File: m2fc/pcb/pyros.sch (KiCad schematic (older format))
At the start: 51 parts, among them P501 CONN_2, P502 CONN_2, P503 CONN_2, Q501 MOSFET_P, Q502 MOSFET_N, Q503 MOSFET_P, Q504 MOSFET_N, Q505 MOSFET_P, Q506 MOSFET_N, U501 HOUSING, U502 HOUSING, U503 HOUSING

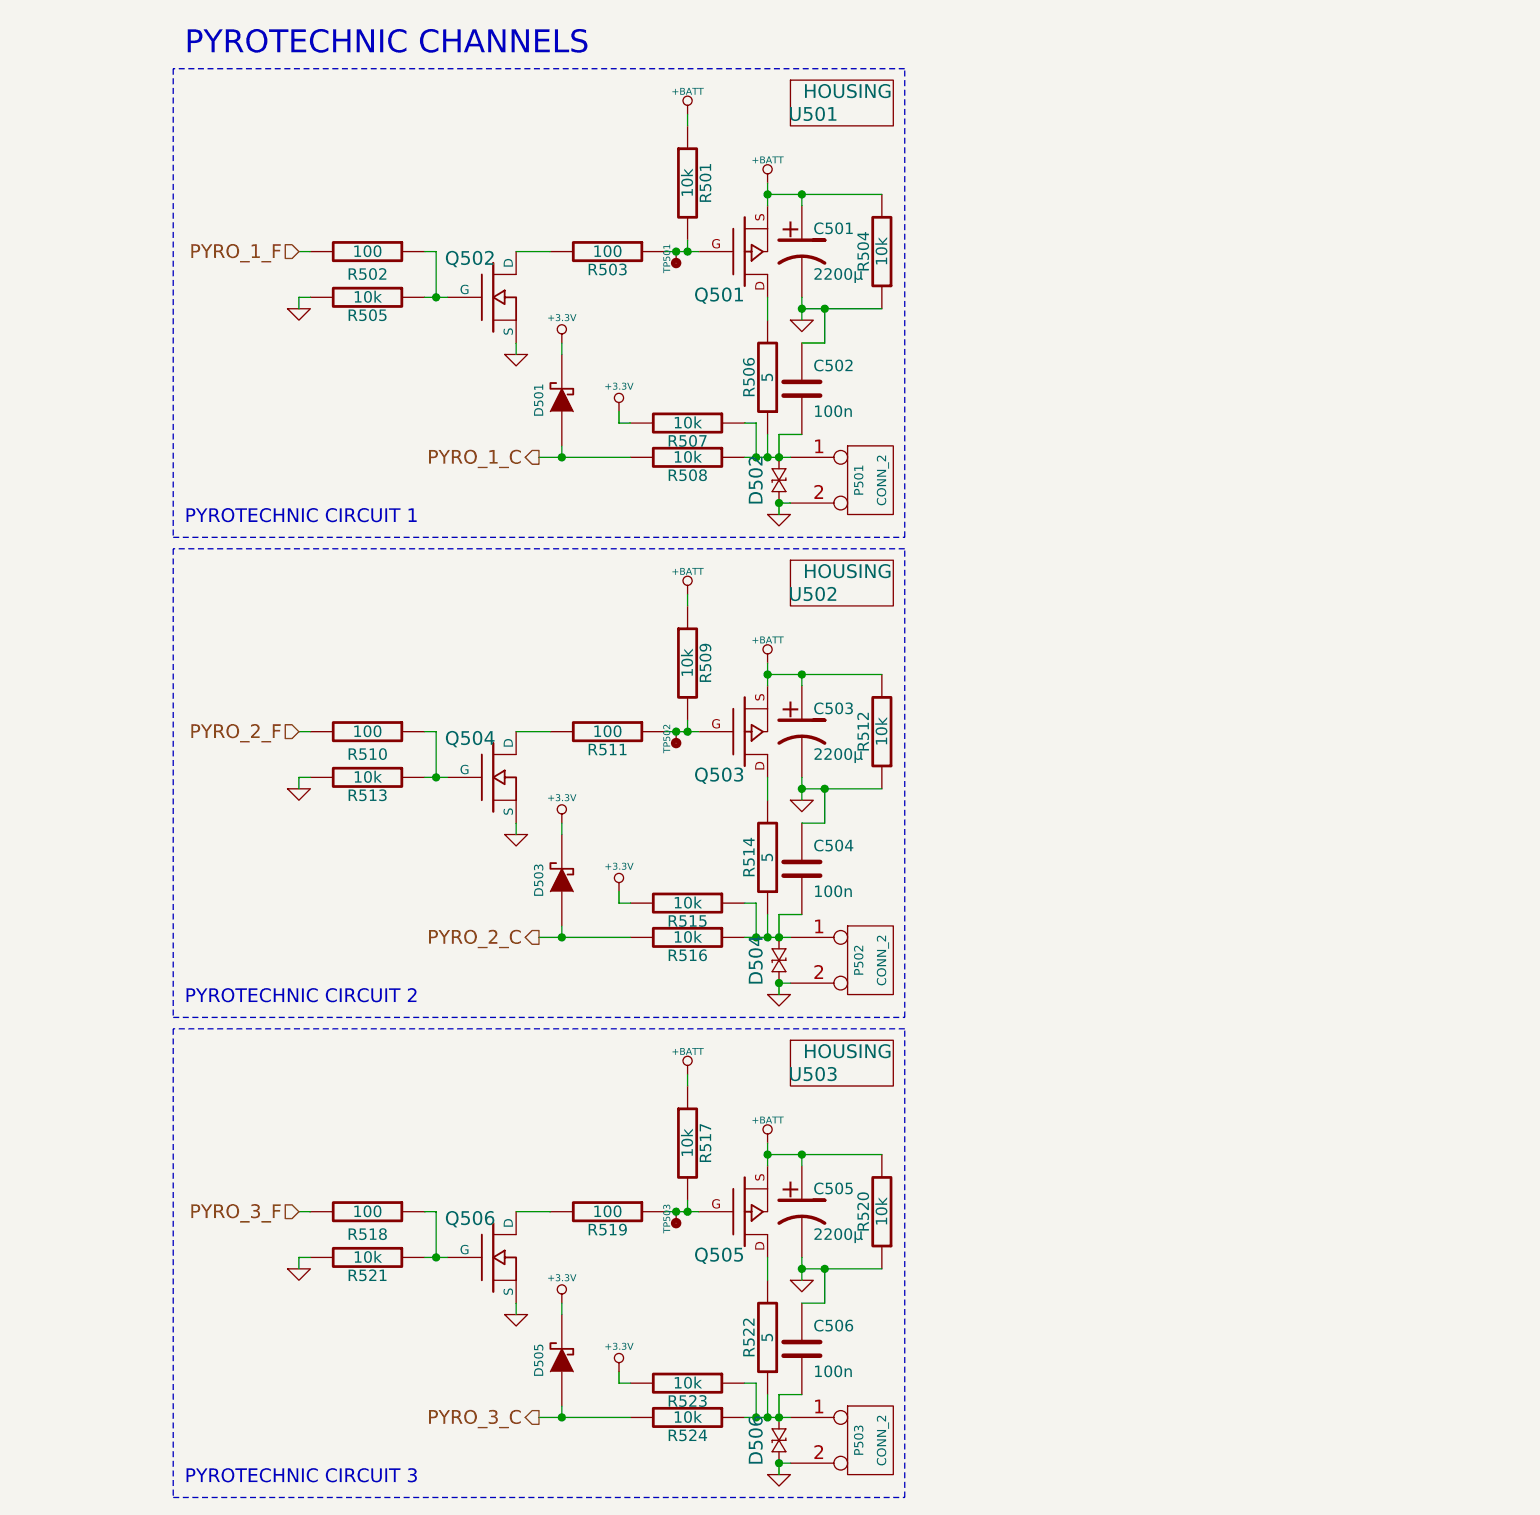
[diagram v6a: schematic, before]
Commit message: m2fc footprints, start layout
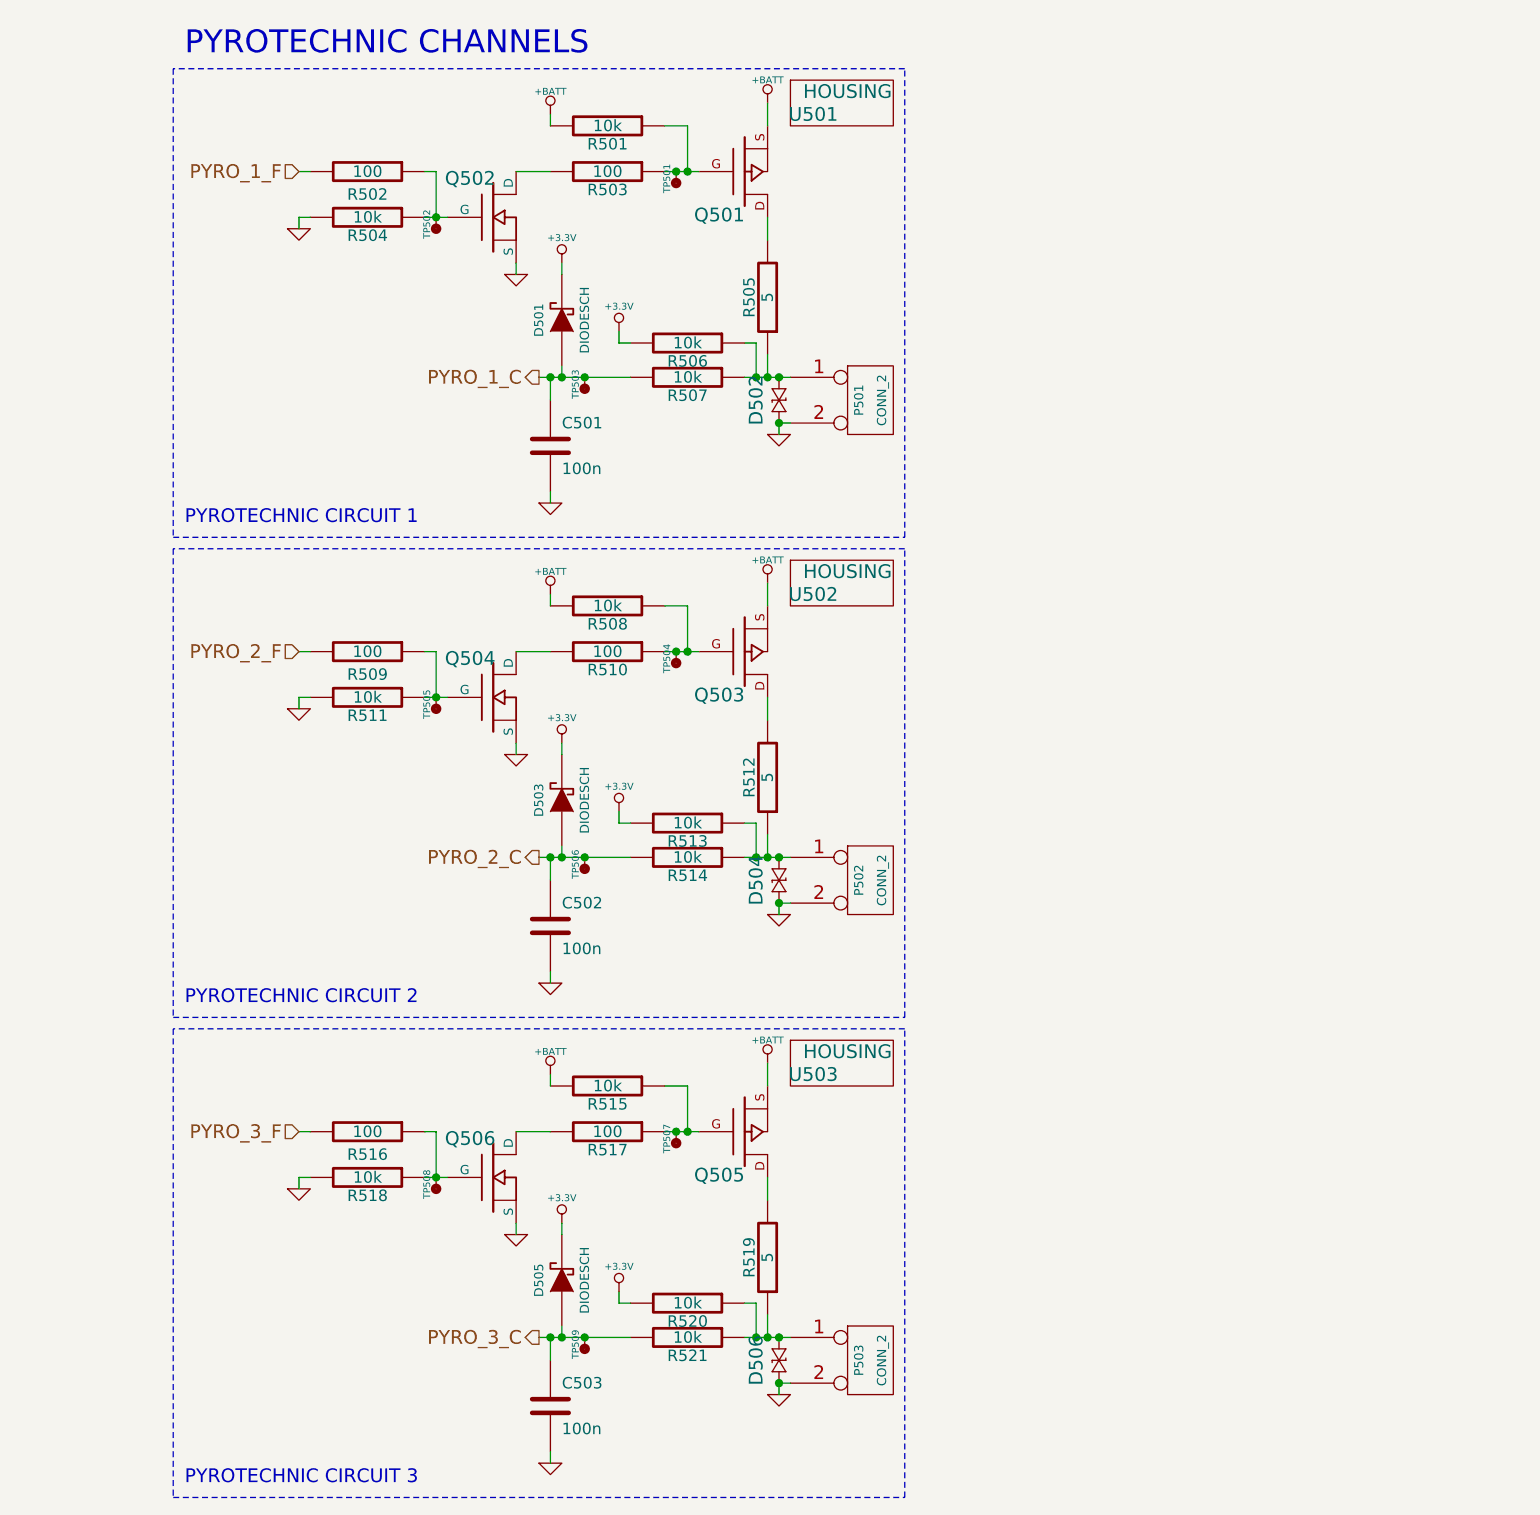
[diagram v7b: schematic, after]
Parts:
- removed C501, C503, C505: 2200µ, symbol CP1
- removed C504, C506: 100n, m2fc:C0603, symbol C
- removed R504, R523, R524: 10k, m2fc:R0603, symbol R
- removed R522: 5, symbol R
- added C501, C503: 100n, m2fc:C0603, symbol C
- added R508: 10k, m2fc:R0603, symbol R
- added TP504, TP505, TP506, TP507, TP508, TP509: TESTPAD, m2fc:TESTPAD, symbol TESTPAD
- D501, D503, D505: footprint SOT-23 -> m2fc:SOD323; Farnell 1056832 -> 1349646
- Q501, Q502, Q503, Q504, Q505, Q506: footprint SOT-23 -> m2fc:SOT-23
- R505: renamed from R506; footprint (none) -> m2fc:PWR4318
- R509, R516, R517: value 10k -> 100; Farnell 2332016 -> 2331989
- R511, R518: value 100 -> 10k; Farnell 2331989 -> 2332016
- R512: value 10k -> 5; footprint m2fc:R0603 -> m2fc:PWR4318; Farnell 2332016 -> 2328356
- R514: value 5 -> 10k; footprint (none) -> m2fc:R0603; Farnell 2328356 -> 2332016
- R519: value 100 -> 5; footprint m2fc:R0603 -> m2fc:PWR4318; Farnell 2331989 -> 2328356
- renumbered R505 to R504, R507 to R506, R508 to R507
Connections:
- net +3.3V: now also R513.2, R520.2; no longer R515.2
- net +BATT: now also R501.2, R515.2, R508.2; no longer R501.1, R509.1, R512.2, R517.1, R520.2
- net GND: now also C502.2, R511.2, R518.2, C501.2, C503.2; no longer C502.1, R512.1, R513.2, R520.1, R521.2
- net PYRO_1_C: now also TP503.1 (TP), C501.1
- net PYRO_2_C: now also C502.1, R514.2, TP506.1 (TP); no longer R516.2
- net PYRO_2_F: now also R509.2; no longer R510.2
- net PYRO_3_C: now also R521.2, C503.1, TP509.1 (TP)
- net PYRO_3_F: now also R516.2; no longer R518.2
- net at Q502.G, R502.1, R504.1: now also TP502.1 (TP)
- net at D502.1, P501.1 (P1), R505.1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: no longer C502.2
- net at Q501.G, R503.1, TP501.1 (TP): now also R501.1; no longer R501.2
- net at D504.1, P502.1 (P1), R514.1: now also R512.1, R513.1; no longer R515.1, R516.1
- net at Q503.D: now also R512.2; no longer R514.2
- net at Q504.D: now also R510.2; no longer R511.2
- net at Q506.G, R518.1: now also R516.1, TP508.1 (TP); no longer R521.1
- net at D506.1, P503.1 (P1): now also R519.1, R520.1, R521.1
- net at Q505.D: now also R519.2
- net at Q506.D: now also R517.2; no longer R519.2
- new net: Q504.G, R509.1, R511.1, TP505.1 (TP)
- new net: Q503.G, R508.1, R510.1, TP504.1 (TP)
- new net: Q505.G, R515.1, R517.1, TP507.1 (TP)
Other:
- moved on the sheet: D502, P501, Q501, Q502, R501, R502, R503, R504, R505, R506, R507, TP501

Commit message: paid off woo
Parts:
- Q501, Q502, Q503, Q504, Q505, Q506: footprint m2fc:SOT-23 -> m2fc:SOT-23-MOSFET
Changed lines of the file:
@@
 PYROTECHNIC CIRCUIT 1
 $Comp
-L GND #PWR0148
+L GND #PWR0153
 U 1 1 53B98AB3
 P 3650 1750
-F 0 "#PWR0148" H 3650 1750 30  0001 C CNN
+F 0 "#PWR0153" H 3650 1750 30  0001 C CNN
 F 1 "GND" H 3650 1680 30  0001 C CNN
 F 2 "" H 3650 1750 60  0001 C CNN
@@
 $EndComp
 $Comp
-L GND #PWR0149
+L GND #PWR0154
 U 1 1 53B98AB9
 P 4600 1950
-F 0 "#PWR0149" H 4600 1950 30  0001 C CNN
+F 0 "#PWR0154" H 4600 1950 30  0001 C CNN
 F 1 "GND" H 4600 1880 30  0001 C CNN
 F 2 "" H 4600 1950 60  0001 C CNN
@@
 $EndComp
 $Comp
-L +BATT #PWR0150
+L +BATT #PWR0155
 U 1 1 53B98AC0
 P 4750 1250
-F 0 "#PWR0150" H 4750 1200 20  0001 C CNN
+F 0 "#PWR0155" H 4750 1200 20  0001 C CNN
 F 1 "+BATT" H 4750 1350 30  0000 C CNN
 F 2 "" H 4750 1250 60  0001 C CNN
@@
 $EndComp
 $Comp
-L +BATT #PWR0151
+L +BATT #PWR0156
 U 1 1 53B98AD4
 P 5700 1200
-F 0 "#PWR0151" H 5700 1150 20  0001 C CNN
+F 0 "#PWR0156" H 5700 1150 20  0001 C CNN
 F 1 "+BATT" H 5700 1300 30  0000 C CNN
 F 2 "" H 5700 1200 60  0001 C CNN
@@
 $EndComp
 $Comp
-L GND #PWR0152
+L GND #PWR0157
 U 1 1 53B98AE0
 P 5750 2650
-F 0 "#PWR0152" H 5750 2650 30  0001 C CNN
+F 0 "#PWR0157" H 5750 2650 30  0001 C CNN
 F 1 "GND" H 5750 2580 30  0001 C CNN
 F 2 "" H 5750 2650 60  0001 C CNN
@@
 F 0 "Q501" H 5600 1690 60  0000 R CNN
 F 1 "MOSFET_P" H 6200 1550 60  0001 R CNN
-F 2 "m2fc:SOT-23" H 5600 1500 60  0001 C CNN
+F 2 "m2fc:SOT-23-MOSFET" H 5600 1500 60  0001 C CNN
 F 3 "" H 5600 1500 60  0001 C CNN
 F 4 "1894738" H 5600 1500 60  0001 C CNN "Farnell"
@@
 F 0 "Q502" H 4510 1870 60  0000 R CNN
 F 1 "MOSFET_N" H 4510 1550 60  0001 R CNN
-F 2 "m2fc:SOT-23" H 4500 1700 60  0001 C CNN
+F 2 "m2fc:SOT-23-MOSFET" H 4500 1700 60  0001 C CNN
 F 3 "" H 4500 1700 60  0001 C CNN
 F 4 "1510761" H 4500 1700 60  0001 C CNN "Farnell"
@@
 $EndComp
 $Comp
-L +3.3V #PWR0153
+L +3.3V #PWR0158
 U 1 1 53C7F0E7
 P 5050 2200
-F 0 "#PWR0153" H 5050 2160 30  0001 C CNN
+F 0 "#PWR0158" H 5050 2160 30  0001 C CNN
 F 1 "+3.3V" H 5050 2310 30  0000 C CNN
 F 2 "" H 5050 2200 60  0000 C CNN
@@
 $EndComp
 $Comp
-L +3.3V #PWR0154
+L +3.3V #PWR0159
 U 1 1 53C7F20C
 P 4800 1900
-F 0 "#PWR0154" H 4800 1860 30  0001 C CNN
+F 0 "#PWR0159" H 4800 1860 30  0001 C CNN
 F 1 "+3.3V" H 4800 2010 30  0000 C CNN
 F 2 "" H 4800 1900 60  0000 C CNN
@@
 Connection ~ 4900 2400
 $Comp
-L GND #PWR0155
+L GND #PWR0160
 U 1 1 53D9528D
 P 4750 2950
-F 0 "#PWR0155" H 4750 2950 30  0001 C CNN
+F 0 "#PWR0160" H 4750 2950 30  0001 C CNN
 F 1 "GND" H 4750 2880 30  0001 C CNN
 F 2 "" H 4750 2950 60  0001 C CNN
@@
 PYROTECHNIC CIRCUIT 2
 $Comp
-L GND #PWR0156
+L GND #PWR0161
 U 1 1 53D96F43
 P 3650 3850
-F 0 "#PWR0156" H 3650 3850 30  0001 C CNN
+F 0 "#PWR0161" H 3650 3850 30  0001 C CNN
 F 1 "GND" H 3650 3780 30  0001 C CNN
 F 2 "" H 3650 3850 60  0001 C CNN
@@
 $EndComp
 $Comp
-L GND #PWR0157
+L GND #PWR0162
 U 1 1 53D96F49
 P 4600 4050
-F 0 "#PWR0157" H 4600 4050 30  0001 C CNN
+F 0 "#PWR0162" H 4600 4050 30  0001 C CNN
 F 1 "GND" H 4600 3980 30  0001 C CNN
 F 2 "" H 4600 4050 60  0001 C CNN
@@
 $EndComp
 $Comp
-L +BATT #PWR0158
+L +BATT #PWR0163
 U 1 1 53D96F4F
 P 4750 3350
-F 0 "#PWR0158" H 4750 3300 20  0001 C CNN
+F 0 "#PWR0163" H 4750 3300 20  0001 C CNN
 F 1 "+BATT" H 4750 3450 30  0000 C CNN
 F 2 "" H 4750 3350 60  0001 C CNN
@@
 $EndComp
 $Comp
-L +BATT #PWR0159
+L +BATT #PWR0164
 U 1 1 53D96F5C
 P 5700 3300
-F 0 "#PWR0159" H 5700 3250 20  0001 C CNN
+F 0 "#PWR0164" H 5700 3250 20  0001 C CNN
 F 1 "+BATT" H 5700 3400 30  0000 C CNN
 F 2 "" H 5700 3300 60  0001 C CNN
@@
 $EndComp
 $Comp
-L GND #PWR0160
+L GND #PWR0165
 U 1 1 53D96F62
 P 5750 4750
-F 0 "#PWR0160" H 5750 4750 30  0001 C CNN
+F 0 "#PWR0165" H 5750 4750 30  0001 C CNN
 F 1 "GND" H 5750 4680 30  0001 C CNN
 F 2 "" H 5750 4750 60  0001 C CNN
@@
 F 0 "Q503" H 5600 3790 60  0000 R CNN
 F 1 "MOSFET_P" H 6200 3650 60  0001 R CNN
-F 2 "m2fc:SOT-23" H 5600 3600 60  0001 C CNN
+F 2 "m2fc:SOT-23-MOSFET" H 5600 3600 60  0001 C CNN
 F 3 "" H 5600 3600 60  0001 C CNN
 F 4 "1894738" H 5600 3600 60  0001 C CNN "Farnell"
@@
 F 0 "Q504" H 4510 3970 60  0000 R CNN
 F 1 "MOSFET_N" H 4510 3650 60  0001 R CNN
-F 2 "m2fc:SOT-23" H 4500 3800 60  0001 C CNN
+F 2 "m2fc:SOT-23-MOSFET" H 4500 3800 60  0001 C CNN
 F 3 "" H 4500 3800 60  0001 C CNN
 F 4 "1510761" H 4500 3800 60  0001 C CNN "Farnell"
@@
 $EndComp
 $Comp
-L +3.3V #PWR0161
+L +3.3V #PWR0166
 U 1 1 53D96FB6
 P 5050 4300
-F 0 "#PWR0161" H 5050 4260 30  0001 C CNN
+F 0 "#PWR0166" H 5050 4260 30  0001 C CNN
 F 1 "+3.3V" H 5050 4410 30  0000 C CNN
 F 2 "" H 5050 4300 60  0000 C CNN
@@
 $EndComp
 $Comp
-L +3.3V #PWR0162
+L +3.3V #PWR0167
 U 1 1 53D96FBC
 P 4800 4000
-F 0 "#PWR0162" H 4800 3960 30  0001 C CNN
+F 0 "#PWR0167" H 4800 3960 30  0001 C CNN
 F 1 "+3.3V" H 4800 4110 30  0000 C CNN
 F 2 "" H 4800 4000 60  0000 C CNN
@@
 Connection ~ 4900 4500
 $Comp
-L GND #PWR0163
+L GND #PWR0168
 U 1 1 53D97008
 P 4750 5050
-F 0 "#PWR0163" H 4750 5050 30  0001 C CNN
+F 0 "#PWR0168" H 4750 5050 30  0001 C CNN
 F 1 "GND" H 4750 4980 30  0001 C CNN
 F 2 "" H 4750 5050 60  0001 C CNN
@@
 PYROTECHNIC CIRCUIT 3
 $Comp
-L GND #PWR0164
+L GND #PWR0169
 U 1 1 53D975FC
 P 3650 5950
-F 0 "#PWR0164" H 3650 5950 30  0001 C CNN
+F 0 "#PWR0169" H 3650 5950 30  0001 C CNN
 F 1 "GND" H 3650 5880 30  0001 C CNN
 F 2 "" H 3650 5950 60  0001 C CNN
@@
 $EndComp
 $Comp
-L GND #PWR0165
+L GND #PWR0170
 U 1 1 53D97602
 P 4600 6150
-F 0 "#PWR0165" H 4600 6150 30  0001 C CNN
+F 0 "#PWR0170" H 4600 6150 30  0001 C CNN
 F 1 "GND" H 4600 6080 30  0001 C CNN
 F 2 "" H 4600 6150 60  0001 C CNN
@@
 $EndComp
 $Comp
-L +BATT #PWR0166
+L +BATT #PWR0171
 U 1 1 53D97608
 P 4750 5450
-F 0 "#PWR0166" H 4750 5400 20  0001 C CNN
+F 0 "#PWR0171" H 4750 5400 20  0001 C CNN
 F 1 "+BATT" H 4750 5550 30  0000 C CNN
 F 2 "" H 4750 5450 60  0001 C CNN
@@
 $EndComp
 $Comp
-L +BATT #PWR0167
+L +BATT #PWR0172
 U 1 1 53D97615
 P 5700 5400
-F 0 "#PWR0167" H 5700 5350 20  0001 C CNN
+F 0 "#PWR0172" H 5700 5350 20  0001 C CNN
 F 1 "+BATT" H 5700 5500 30  0000 C CNN
 F 2 "" H 5700 5400 60  0001 C CNN
@@
 $EndComp
 $Comp
-L GND #PWR0168
+L GND #PWR0173
 U 1 1 53D9761B
 P 5750 6850
-F 0 "#PWR0168" H 5750 6850 30  0001 C CNN
+F 0 "#PWR0173" H 5750 6850 30  0001 C CNN
 F 1 "GND" H 5750 6780 30  0001 C CNN
 F 2 "" H 5750 6850 60  0001 C CNN
@@
 F 0 "Q505" H 5600 5890 60  0000 R CNN
 F 1 "MOSFET_P" H 6200 5750 60  0001 R CNN
-F 2 "m2fc:SOT-23" H 5600 5700 60  0001 C CNN
+F 2 "m2fc:SOT-23-MOSFET" H 5600 5700 60  0001 C CNN
 F 3 "" H 5600 5700 60  0001 C CNN
 F 4 "1894738" H 5600 5700 60  0001 C CNN "Farnell"
@@
 F 0 "Q506" H 4510 6070 60  0000 R CNN
 F 1 "MOSFET_N" H 4510 5750 60  0001 R CNN
-F 2 "m2fc:SOT-23" H 4500 5900 60  0001 C CNN
+F 2 "m2fc:SOT-23-MOSFET" H 4500 5900 60  0001 C CNN
 F 3 "" H 4500 5900 60  0001 C CNN
 F 4 "1510761" H 4500 5900 60  0001 C CNN "Farnell"
@@
 $EndComp
 $Comp
-L +3.3V #PWR0169
+L +3.3V #PWR0174
 U 1 1 53D9766F
 P 5050 6400
-F 0 "#PWR0169" H 5050 6360 30  0001 C CNN
+F 0 "#PWR0174" H 5050 6360 30  0001 C CNN
 F 1 "+3.3V" H 5050 6510 30  0000 C CNN
 F 2 "" H 5050 6400 60  0000 C CNN
@@
 $EndComp
 $Comp
-L +3.3V #PWR0170
+L +3.3V #PWR0175
 U 1 1 53D97675
 P 4800 6100
-F 0 "#PWR0170" H 4800 6060 30  0001 C CNN
+F 0 "#PWR0175" H 4800 6060 30  0001 C CNN
 F 1 "+3.3V" H 4800 6210 30  0000 C CNN
 F 2 "" H 4800 6100 60  0000 C CNN
@@
 Connection ~ 4900 6600
 $Comp
-L GND #PWR0171
+L GND #PWR0176
 U 1 1 53D976C1
 P 4750 7150
-F 0 "#PWR0171" H 4750 7150 30  0001 C CNN
+F 0 "#PWR0176" H 4750 7150 30  0001 C CNN
 F 1 "GND" H 4750 7080 30  0001 C CNN
 F 2 "" H 4750 7150 60  0001 C CNN
